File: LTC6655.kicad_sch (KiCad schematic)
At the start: 5 parts, among them U2801 LTC6655CHLS8-2.5#PBF

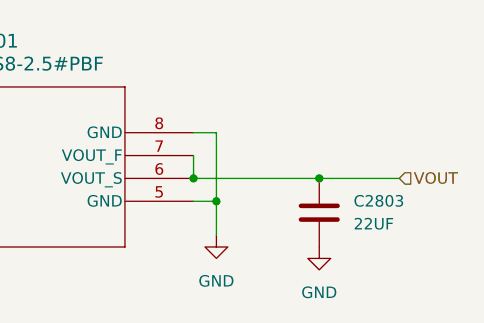
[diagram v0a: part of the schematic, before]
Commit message: Updates from Michal to fix ERC errors
Still lots of ERC warnings
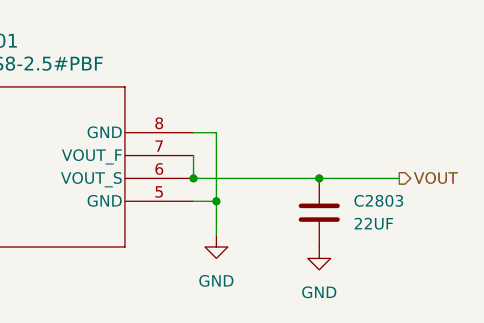
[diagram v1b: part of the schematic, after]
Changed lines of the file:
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@@
 	)
 	(hierarchical_label "VOUT"
-		(shape input)
+		(shape output)
 		(at 177.8 88.9 0)
 		(fields_autoplaced yes)

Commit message: Schematic Changes
Added Manufacturer/MPN/Description Fields to parts
Added libraries to project
Modified FMC schematic to use new symbol
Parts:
- C2801: Manufacturer (none) -> Murata; Manufacturer Part Number (none) -> GRM188R61E105KA12D
- C2802: Manufacturer (none) -> Murata; Manufacturer Part Number (none) -> GRM31CR61A476ME15L
- C2803: Manufacturer (none) -> Panasonic; Manufacturer Part Number (none) -> EEF-CD1B220R
- FB2801: Manufacturer (none) -> Würth; Manufacturer Part Number (none) -> 742792040
- U2801: Manufacturer (none) -> Analog Devices; Manufacturer Part Number (none) -> LTC6655CHLS8-2.5#PBF
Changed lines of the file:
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@@
 			)
 		)
-		(property "Description" "Al-Poly"
+		(property "Description" "CAP ALUM POLY 22UF 20% 12.5V SMD"
 			(at 168.91 92.71 0)
 			(effects
@@
 		(property "Vendor" "digikey:PCE3168CT-ND"
 			(at 0 185.42 0)
+			(effects
+				(font
+					(size 1.27 1.27)
+				)
+				(hide yes)
+			)
+		)
+		(property "Manufacturer" "Panasonic"
+			(at 168.91 92.71 0)
+			(effects
+				(font
+					(size 1.27 1.27)
+				)
+				(hide yes)
+			)
+		)
+		(property "Manufacturer Part Number" "EEF-CD1B220R "
+			(at 168.91 92.71 0)
 			(effects
 				(font
@@
 			)
 		)
-		(property "Description" "Ferrite bead"
+		(property "Description" "FERRITE BEAD 600 OHM 0805 1LN"
 			(at 64.77 81.28 0)
 			(effects
@@
 		(property "Vendor" "digikey:732-1620-1-ND"
 			(at -16.51 16.51 0)
+			(effects
+				(font
+					(size 1.27 1.27)
+				)
+				(hide yes)
+			)
+		)
+		(property "Manufacturer" "Würth"
+			(at 64.77 81.28 0)
+			(effects
+				(font
+					(size 1.27 1.27)
+				)
+				(hide yes)
+			)
+		)
+		(property "Manufacturer Part Number" "742792040"
+			(at 64.77 81.28 0)
 			(effects
 				(font
@@
 			)
 		)
-		(property "Description" ""
+		(property "Description" "IC VREF SERIES 0.05% 8CLCC"
 			(at 109.22 83.82 0)
 			(effects
@@
 		(property "Vendor" "digikey:LTC6655CHLS8-2.5#PBF-ND"
 			(at 0 167.64 0)
+			(effects
+				(font
+					(size 1.27 1.27)
+				)
+				(hide yes)
+			)
+		)
+		(property "Manufacturer" "Analog Devices"
+			(at 109.22 83.82 0)
+			(effects
+				(font
+					(size 1.27 1.27)
+				)
+				(hide yes)
+			)
+		)
+		(property "Manufacturer Part Number" "LTC6655CHLS8-2.5#PBF "
+			(at 109.22 83.82 0)
 			(effects
 				(font
@@
 			)
 		)
-		(property "Description" "Unpolarized capacitor"
+		(property "Description" "CAP CER 1UF 25V X5R 0603"
 			(at 77.47 88.9 0)
 			(effects
@@
 		(property "Vendor" "digikey:490-3897-1-ND"
 			(at 154.94 0 0)
+			(effects
+				(font
+					(size 1.27 1.27)
+				)
+				(hide yes)
+			)
+		)
+		(property "Manufacturer" "Murata"
+			(at 77.47 88.9 0)
+			(effects
+				(font
+					(size 1.27 1.27)
+				)
+				(hide yes)
+			)
+		)
+		(property "Manufacturer Part Number" "GRM188R61E105KA12D"
+			(at 77.47 88.9 0)
 			(effects
 				(font
@@
 			)
 		)
-		(property "Description" "Unpolarized capacitor"
+		(property "Description" "CAP CER 47UF 10V X5R 1206"
 			(at 90.17 88.9 0)
 			(effects
@@
 			(effects
 				(font
+					(size 1.27 1.27)
+				)
+				(hide yes)
+			)
+		)
+		(property "Manufacturer" "Murata"
+			(at 90.17 88.9 0)
+			(effects
+				(font
+					(size 1.27 1.27)
+				)
+				(hide yes)
+			)
+		)
+		(property "Manufacturer Part Number" "GRM31CR61A476ME15L "
+			(at 90.17 88.9 0)
+			(effects
+				(font

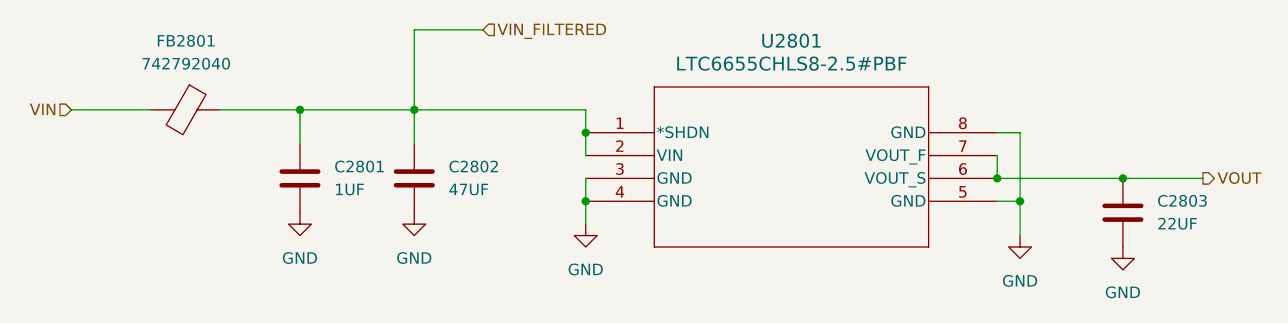
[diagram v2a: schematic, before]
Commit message: Schematics update
Cleaned up RF ADC and front end sections.
Verified that changes did not changes anything about the layout.
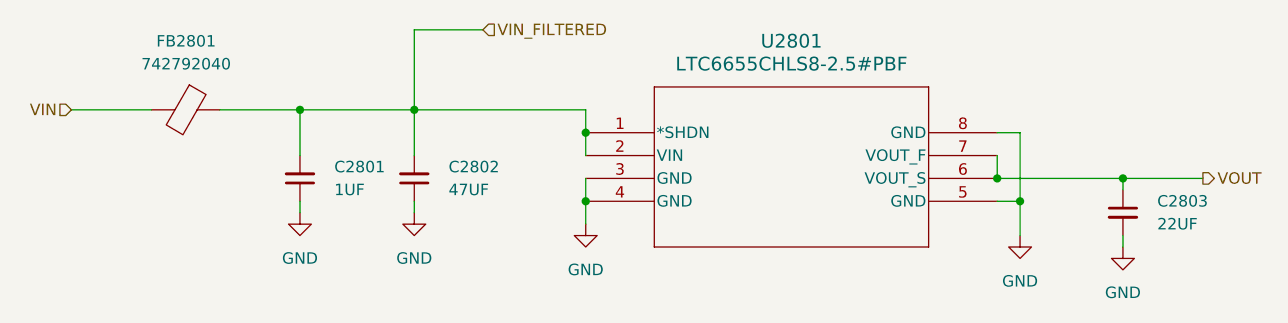
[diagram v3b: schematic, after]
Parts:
- C2801, C2802, C2803: symbol Device:C -> Device:C_Small
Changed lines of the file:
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@@
+	)
+	(junction
+		(at 157.48 91.44)
+		(diameter 0)
+		(color 0 0 0 0)
+	)
+	(junction
+		(at 154.94 88.9)
+		(diameter 0)
+		(color 0 0 0 0)
+	)
+	(junction
+		(at 109.22 83.82)
+		(diameter 0)
+		(color 0 0 0 0)
 	)
 	(junction
@@
 	)
 	(junction
-		(at 157.48 91.44)
-		(diameter 0)
-		(color 0 0 0 0)
-	)
-	(junction
-		(at 154.94 88.9)
-		(diameter 0)
-		(color 0 0 0 0)
-	)
-	(junction
-		(at 109.22 83.82)
-		(diameter 0)
-		(color 0 0 0 0)
-	)
-	(junction
 		(at 77.47 81.28)
 		(diameter 0)
@@
 	(wire
 		(pts
-			(xy 77.47 81.28) (xy 77.47 85.09)
+			(xy 77.47 81.28) (xy 77.47 86.36)
+		)
+		(stroke
+			(width 0)
+			(type default)
+		)
+	)
+	(wire
+		(pts
+			(xy 77.47 91.44) (xy 77.47 92.71)
 		)
 		(stroke
@@
 	(wire
 		(pts
+			(xy 168.91 95.25) (xy 168.91 96.52)
+		)
+		(stroke
+			(width 0)
+			(type default)
+		)
+	)
+	(wire
+		(pts
 			(xy 109.22 88.9) (xy 109.22 91.44)
 		)
@@
 	(wire
 		(pts
+			(xy 90.17 91.44) (xy 90.17 92.71)
+		)
+		(stroke
+			(width 0)
+			(type default)
+		)
+	)
+	(wire
+		(pts
 			(xy 154.94 86.36) (xy 154.94 88.9)
 		)
@@
 	(wire
 		(pts
-			(xy 90.17 81.28) (xy 90.17 85.09)
+			(xy 90.17 81.28) (xy 90.17 86.36)
+		)
+		(stroke
+			(width 0)
+			(type default)
+		)
+	)
+	(wire
+		(pts
+			(xy 168.91 90.17) (xy 168.91 88.9)
 		)
 		(stroke
@@
 	)
 	(symbol
-		(lib_id "Device:C")
+		(lib_id "Device:C_Small")
 		(at 168.91 92.71 0)
 		(unit 1)
@@
 	)
 	(symbol
-		(lib_id "Device:C")
+		(lib_id "Device:C_Small")
 		(at 77.47 88.9 180)
 		(unit 1)
@@
 	)
 	(symbol
-		(lib_id "Device:C")
+		(lib_id "Device:C_Small")
 		(at 90.17 88.9 180)
 		(unit 1)
